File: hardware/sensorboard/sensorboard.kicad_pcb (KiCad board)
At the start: 2 copper layers, 51.7 x 19.1 mm, 23 parts, among them P1 PWR, P2 PROG, U1 ESP-07v2, U2 LMR16006Y, U3 BMP180_board, U4 DHT22

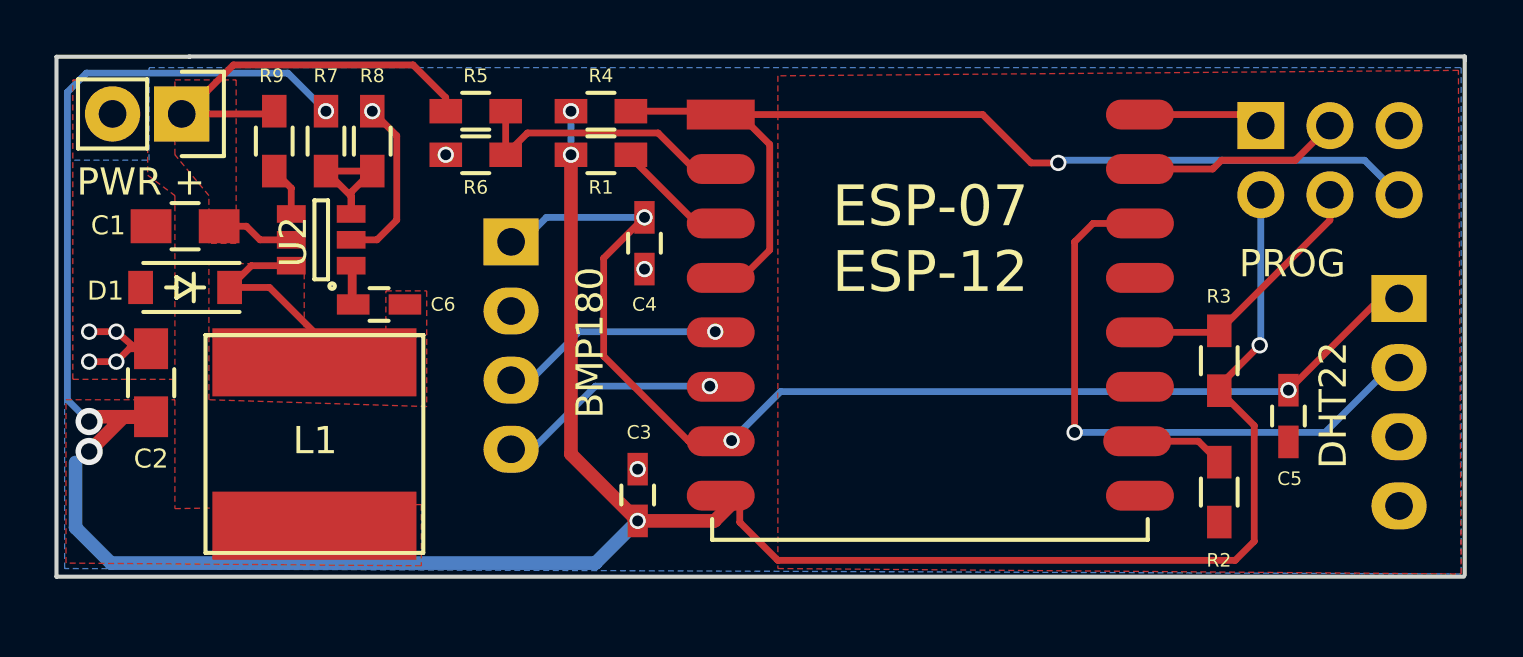
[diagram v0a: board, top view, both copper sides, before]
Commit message: Use smaller inductor, shrink board a little
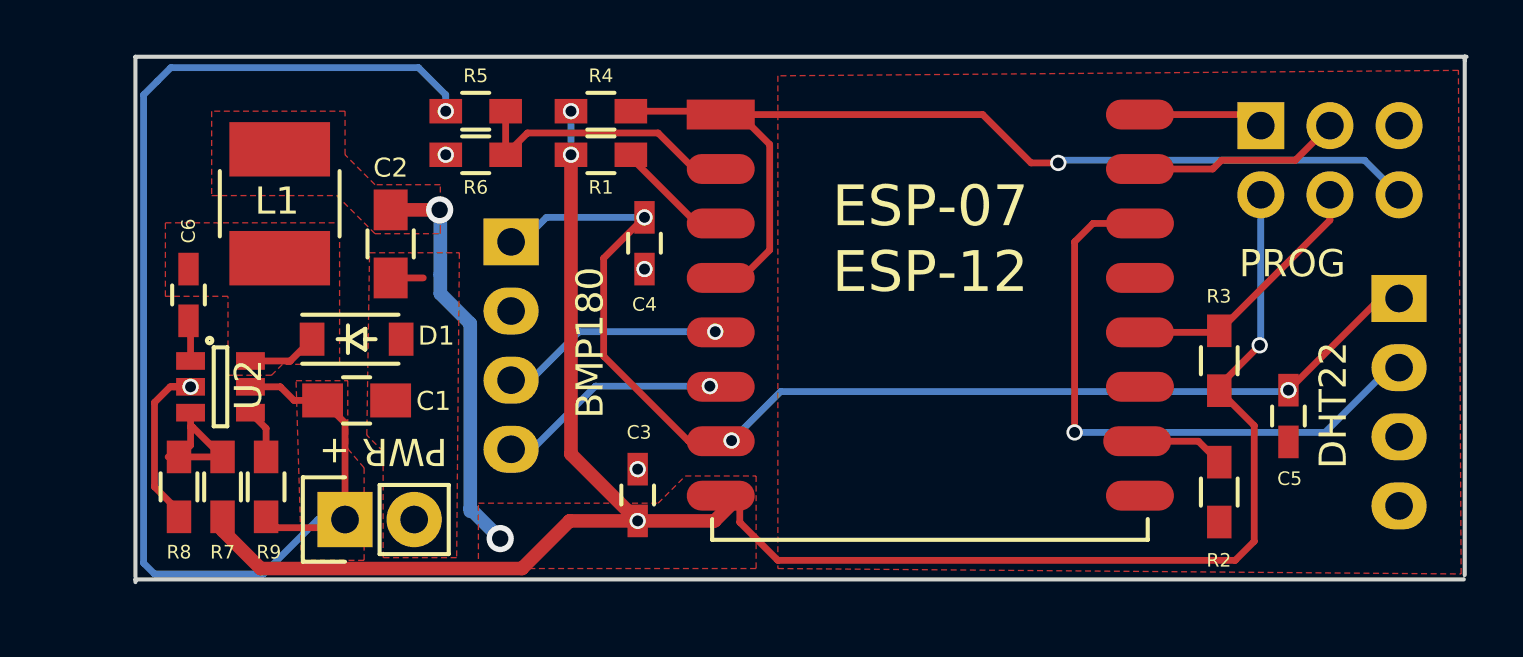
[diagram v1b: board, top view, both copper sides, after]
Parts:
- L1: footprint Inductors:NR8040_HandSoldering -> Inductors:NR4018_HandSoldering
- moved P1 16.1 mm to (134.0, 89.4), turned to 90 degrees
- moved R8 14.5 mm to (127.9, 88.2), turned to 270 degrees
- moved R7 13.3 mm to (129.5, 88.2), turned to 90 degrees
- moved R9 12.7 mm to (131.1, 88.2), turned to 90 degrees
- moved C2 10.2 mm to (135.7, 79.3), turned to 270 degrees
- moved C1 8.98 mm to (134.4, 85.0), turned to 0 degrees
- moved L1 8.92 mm to (131.6, 77.8), turned to 90 degrees
- moved C6 7.01 mm to (128.2, 81.2), turned to 90 degrees
- moved D1 6.58 mm to (134.4, 82.8), turned to 0 degrees
- moved U2 6.55 mm to (129.4, 84.5), turned to 0 degrees
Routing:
- net +6V: track 18.2 -> 48.8 mm, vias 0 -> 1
- net +3V3: track 108.4 -> 86.8 mm, vias 7 -> 6
- net Net-(C6-Pad2): track 7.49 -> 2.60 mm
- net GND: track 11.8 -> 8.54 mm, vias 8 -> 4
- net Net-(C6-Pad1): track 2.91 -> 1.51 mm
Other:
- board size 51.7 x 19.1 mm -> 48.9 x 19.3 mm

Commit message: Fix some silkscreens
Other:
- board text added: "ESP sensorboard v3.1"
- board text removed: "ESP sensorboard v3.0"
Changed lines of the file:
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@@
     (pad_to_mask_clearance 0.2)
     (aux_axis_origin 0 0)
+    (grid_origin 143.2 70.1236)
     (visible_elements FFFEFF7F)
     (pcbplotparams
@@
     (effects (font (size 0.7 0.7) (thickness 0.15)) (justify mirror))
   )
-  (gr_text "ESP sensorboard v3.0" (at 151.2 74.1) (layer B.SilkS)
+  (gr_text "ESP sensorboard v3.1" (at 151.2 74.1) (layer B.SilkS)
     (effects (font (size 1.5 1.5) (thickness 0.3)) (justify mirror))
   )

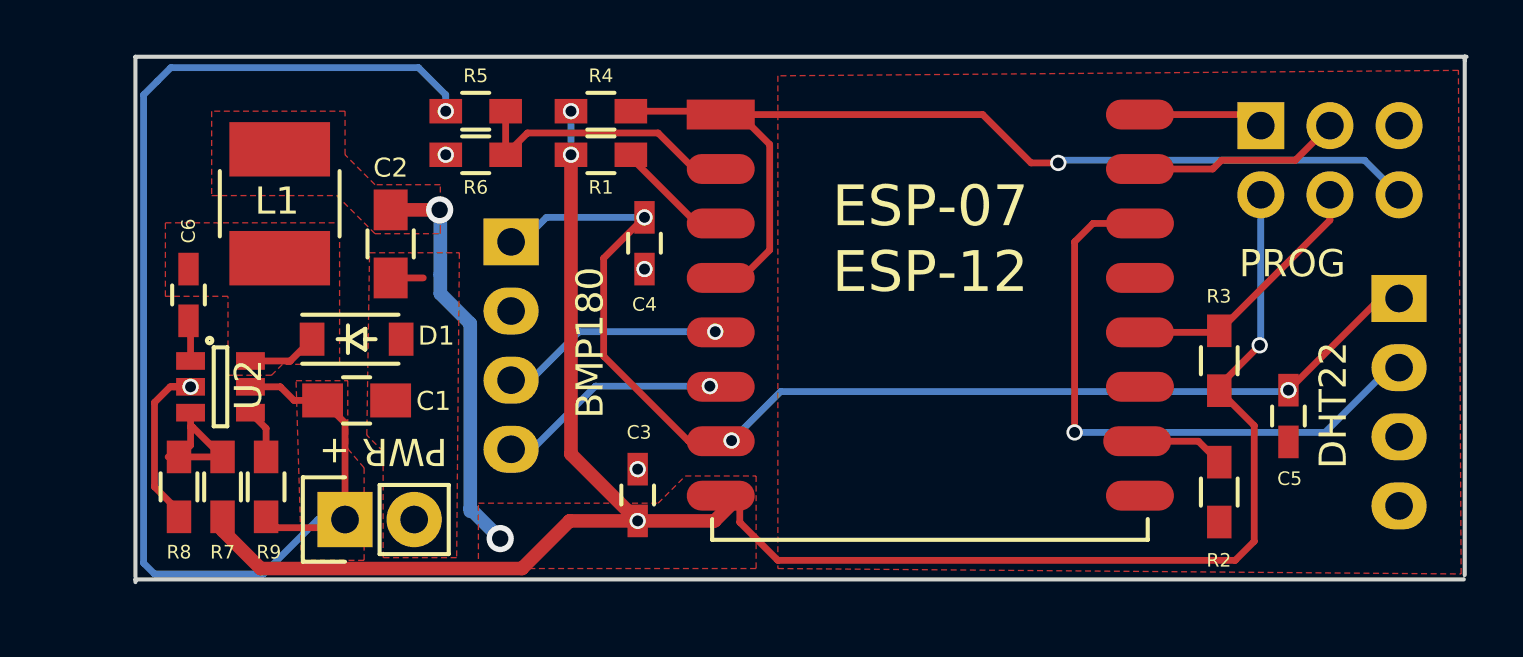
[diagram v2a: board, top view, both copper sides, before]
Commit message: Better routing of 3v3
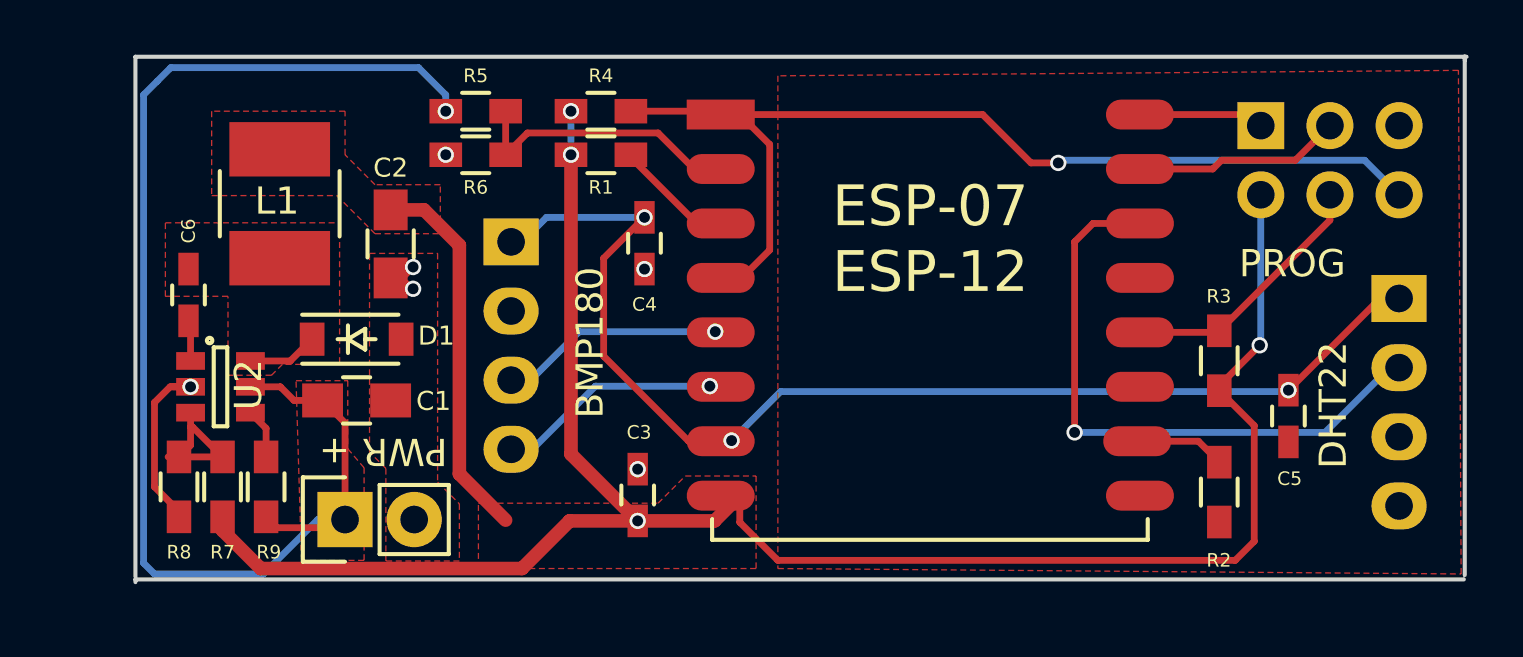
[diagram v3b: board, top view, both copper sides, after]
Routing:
- net +3V3: track 86.8 -> 85.8 mm, vias 6 -> 4
- net GND: track 8.54 -> 9.30 mm, vias 4 -> 6
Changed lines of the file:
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@@
     (thickness 1.6)
     (drawings 20)
-    (tracks 144)
+    (tracks 143)
     (zones 0)
     (modules 23)
@@
   (segment (start 134 89.7) (end 131.5 89.7) (width 0.25) (layer F.Cu) (net 1))
   (segment (start 131.5 89.7) (end 131.1 89.3) (width 0.25) (layer F.Cu) (net 1))
-  (segment (start 135.675 80.525) (end 136.875 80.525) (width 0.25) (layer F.Cu) (net 2) (status 400000))
+  (segment (start 135.675 80.525) (end 136.0014 80.525) (width 0.25) (layer F.Cu) (net 2) (status C00000))
+  (segment (start 136.0014 80.525) (end 136.5 80.9236) (width 0.25) (layer F.Cu) (net 2))
+  (via (at 136.5 80.9236) (size 0.6) (drill 0.4) (layers F.Cu B.Cu) (net 2))
+  (segment (start 135.675 80.525) (end 136.0986 80.525) (width 0.25) (layer F.Cu) (net 2) (status C00000))
+  (segment (start 136.0986 80.525) (end 136.5 80.1236) (width 0.25) (layer F.Cu) (net 2) (status 400000))
+  (via (at 136.5 80.1236) (size 0.6) (drill 0.4) (layers F.Cu B.Cu) (net 2))
   (via (at 137.7 76) (size 0.6) (drill 0.4) (layers F.Cu B.Cu) (net 2))
   (via (at 128.325 84.525) (size 0.6) (drill 0.4) (layers F.Cu B.Cu) (net 2))
@@
   (segment (start 144.75 87.55) (end 144.7 87.6) (width 0.25) (layer B.Cu) (net 2))
   (via (at 145 80.2) (size 0.6) (drill 0.4) (layers F.Cu B.Cu) (net 2))
+  (segment (start 135.675 78.025) (end 136.9014 78.025) (width 0.5) (layer F.Cu) (net 3) (status 400000))
+  (segment (start 138.2 87.7236) (end 139.9 89.4236) (width 0.5) (layer F.Cu) (net 3))
+  (segment (start 138.2 79.3236) (end 138.2 87.7236) (width 0.5) (layer F.Cu) (net 3))
+  (segment (start 136.9014 78.025) (end 138.2 79.3236) (width 0.5) (layer F.Cu) (net 3))
   (segment (start 130.9 91.2) (end 140.5 91.2) (width 0.5) (layer F.Cu) (net 3))
   (segment (start 129.5 89.8) (end 130.9 91.2) (width 0.5) (layer F.Cu) (net 3))
   (segment (start 142.25 89.45) (end 144.75 89.45) (width 0.5) (layer F.Cu) (net 3))
   (segment (start 140.5 91.2) (end 142.25 89.45) (width 0.5) (layer F.Cu) (net 3))
-  (segment (start 138.6 89) (end 139.7 90.1) (width 0.5) (layer B.Cu) (net 3))
-  (via (at 139.7 90.1) (size 1) (drill 0.6) (layers F.Cu B.Cu) (net 3))
-  (via (at 137.475 78.025) (size 1) (drill 0.6) (layers F.Cu B.Cu) (net 3))
-  (segment (start 137.475 78.025) (end 137.5 78) (width 0.5) (layer B.Cu) (net 3))
   (segment (start 129.5 89.3) (end 129.5 89.8) (width 0.5) (layer F.Cu) (net 3))
-  (segment (start 135.675 78.025) (end 137.475 78.025) (width 0.5) (layer F.Cu) (net 3))
   (via (at 144.75 89.45) (size 0.6) (drill 0.4) (layers F.Cu B.Cu) (net 3))
-  (segment (start 137.5 78) (end 137.5 80.4) (width 0.5) (layer B.Cu) (net 3))
-  (segment (start 137.5 80.4) (end 137.5 81.1) (width 0.5) (layer B.Cu) (net 3))
-  (segment (start 137.5 81.1) (end 138.6 82.2) (width 0.5) (layer B.Cu) (net 3))
-  (segment (start 138.6 82.2) (end 138.6 89) (width 0.5) (layer B.Cu) (net 3))
-  (segment (start 138.6 89) (end 138.6 89.1) (width 0.5) (layer B.Cu) (net 3))
   (segment (start 142.3 76) (end 142.3 87) (width 0.5) (layer F.Cu) (net 3))
   (segment (start 142.3 87) (end 144.75 89.45) (width 0.5) (layer F.Cu) (net 3))
@@
     )
   )
-  (zone (net 2) (net_name GND) (layer F.Cu) (hatch edge 0.508)
-    (connect_pads yes (clearance 0.508))
-    (min_thickness 0.254)
-    (fill yes (arc_segments 16) (thermal_gap 0.508) (thermal_bridge_width 0.508))
-    (polygon
-      (pts
-        (xy 138.1 90.8) (xy 135.4 90.8) (xy 135.4 86.9) (xy 134.8 86.3) (xy 134.9 79.6)
-        (xy 138.2 79.6) (xy 138.1 90.8)
-      )
-    )
-  )
   (zone (net 3) (net_name +3V3) (layer F.Cu) (hatch edge 0.508)
     (connect_pads yes (clearance 0.508))
@@
       )
     )
+  )
+  (zone (net 2) (net_name GND) (layer F.Cu) (hatch edge 0.508)
+    (connect_pads yes (clearance 0.508))
+    (min_thickness 0.254)
+    (fill yes (arc_segments 16) (thermal_gap 0.508) (thermal_bridge_width 0.508))
+    (polygon
+      (pts
+        (xy 137.4 88.0236) (xy 138.2 88.8236) (xy 138.2 90.9236) (xy 135.5 90.9236) (xy 135.5 87.5236)
+        (xy 134.9 86.9236) (xy 134.9 79.6236) (xy 137.4 79.6236) (xy 137.4 88.0236)
+      )
+    )

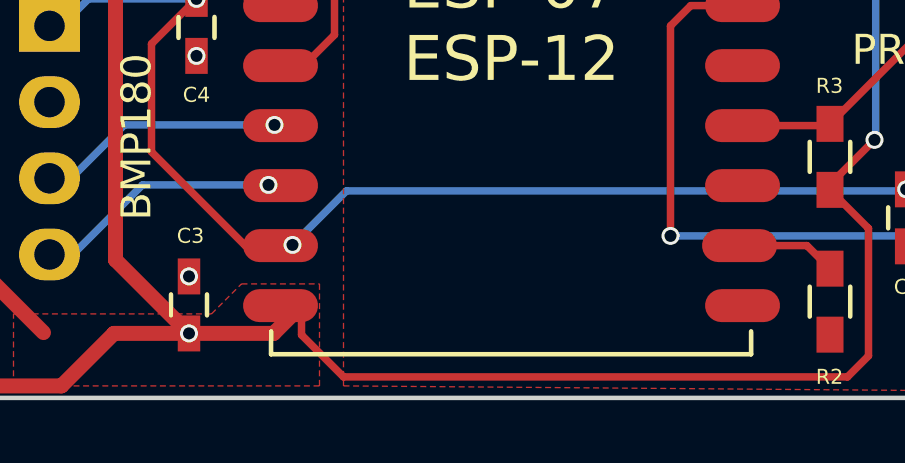
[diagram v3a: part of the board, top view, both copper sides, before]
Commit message: Remove extra 3v3 via, add better ground connection
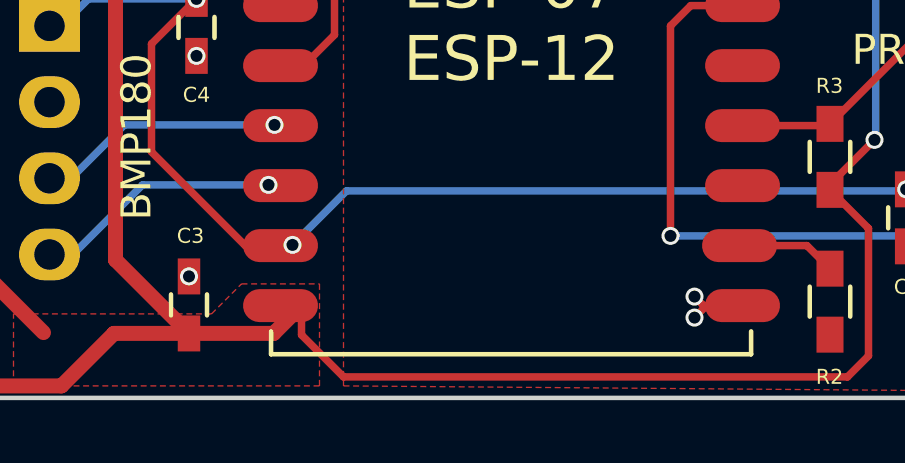
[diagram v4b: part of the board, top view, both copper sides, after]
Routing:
- net GND: track 9.30 -> 11.4 mm, vias 6 -> 8
- net +3V3: vias 4 -> 3
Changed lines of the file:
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@@
     (thickness 1.6)
     (drawings 20)
-    (tracks 143)
+    (tracks 148)
     (zones 0)
     (modules 23)
@@
   (segment (start 134 89.7) (end 131.5 89.7) (width 0.25) (layer F.Cu) (net 1))
   (segment (start 131.5 89.7) (end 131.1 89.3) (width 0.25) (layer F.Cu) (net 1))
+  (segment (start 162.5011 88.5236) (end 162 88.5236) (width 0.25) (layer F.Cu) (net 2) (status C00000))
+  (segment (start 162 88.5236) (end 161.6 88.9236) (width 0.25) (layer F.Cu) (net 2) (status 400000))
+  (via (at 161.6 88.9236) (size 0.6) (drill 0.4) (layers F.Cu B.Cu) (net 2))
+  (segment (start 162.5011 88.5236) (end 161.9 88.5236) (width 0.25) (layer F.Cu) (net 2) (status 400000))
+  (via (at 161.6 88.2236) (size 0.6) (drill 0.4) (layers F.Cu B.Cu) (net 2))
+  (segment (start 161.9 88.5236) (end 161.6 88.2236) (width 0.25) (layer F.Cu) (net 2))
   (segment (start 135.675 80.525) (end 136.0014 80.525) (width 0.25) (layer F.Cu) (net 2) (status C00000))
   (segment (start 136.0014 80.525) (end 136.5 80.9236) (width 0.25) (layer F.Cu) (net 2))
@@
   (segment (start 140.5 91.2) (end 142.25 89.45) (width 0.5) (layer F.Cu) (net 3))
   (segment (start 129.5 89.3) (end 129.5 89.8) (width 0.5) (layer F.Cu) (net 3))
-  (via (at 144.75 89.45) (size 0.6) (drill 0.4) (layers F.Cu B.Cu) (net 3))
   (segment (start 142.3 76) (end 142.3 87) (width 0.5) (layer F.Cu) (net 3))
   (segment (start 142.3 87) (end 144.75 89.45) (width 0.5) (layer F.Cu) (net 3))
